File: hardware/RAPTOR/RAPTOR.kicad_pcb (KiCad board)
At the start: 2 copper layers, 88.9 x 53.3 mm, 47 parts, among them J1 SOLC_CONN, J10 EXT_LED3, J11 SRVOL_CONN, J12 SRVOR_CONN, J13 HOTWIRE_CONN, J14 RBF_CONN, J15 EEPROM_BTN_CONN, J16 SOLC_SW_CONN, J17 SOLP_SW_CONN, J2 SOLP_CONN, J3 JST_2MM_MALE, J4 CONN_LED_FIX, J5 CONN_SOLP_LED, J6 CONN_SOLC_LED, J7 EXT_LED0, J8 EXT_LED1, J9 EXT_LED2, P1 Power, P2 Analog, P3 Digital, P4 Digital, P5 CONN_01X01, P6 CONN_01X01, P7 CONN_01X01, P8 CONN_01X01, Q1 MOSFET-NCH-2N7002PW, Q2 MOSFET-NCH-2N7002PW, Q3 MOSFET-NCH-2N7002PW, Q4 MOSFET-NCH-2N7002PW, Q5 MOSFET-NCH-2N7002PW, U1 BMP280 Breakout, U2 BNO055 Breakout, U3 OpenLog, U4 AdafruitGPS, U5 U3V12F12, U6 D24V550F5

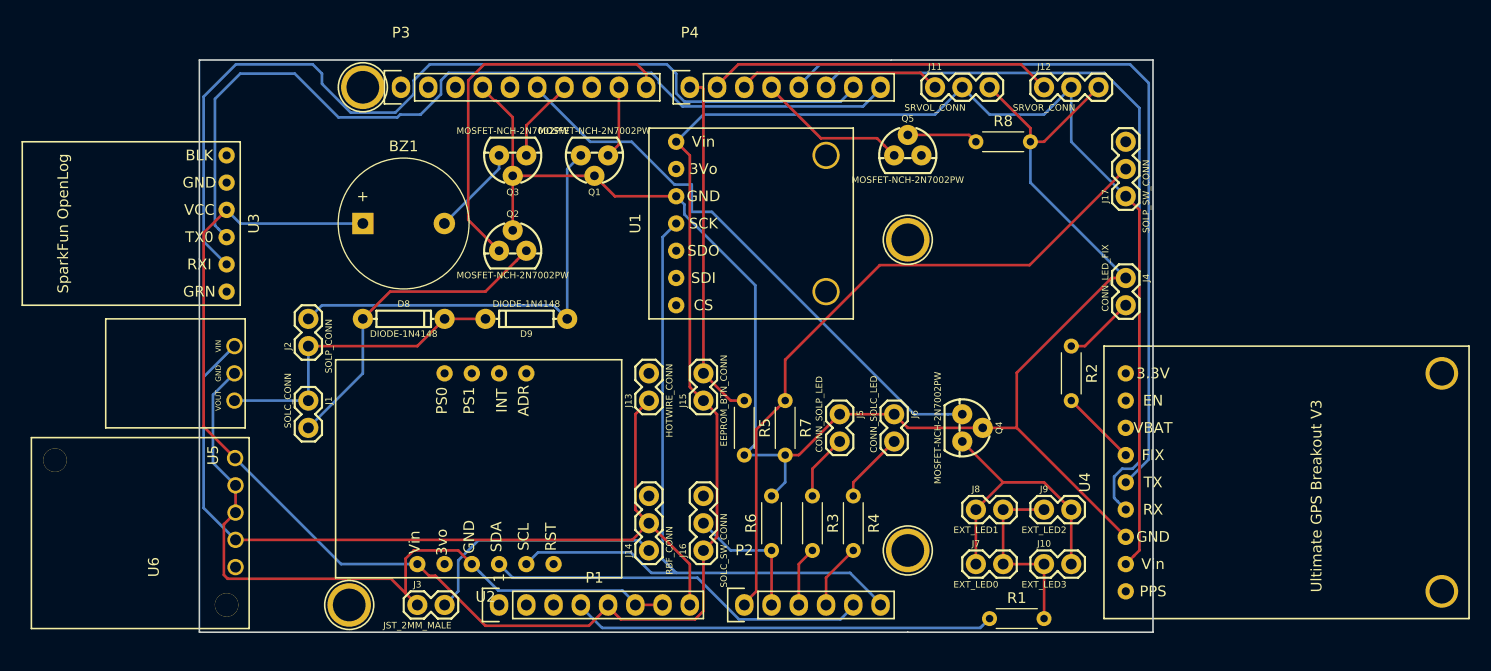
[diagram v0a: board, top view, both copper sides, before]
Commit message: Version 1 of fully wired PCB
A preliminary full connection of the PCB board
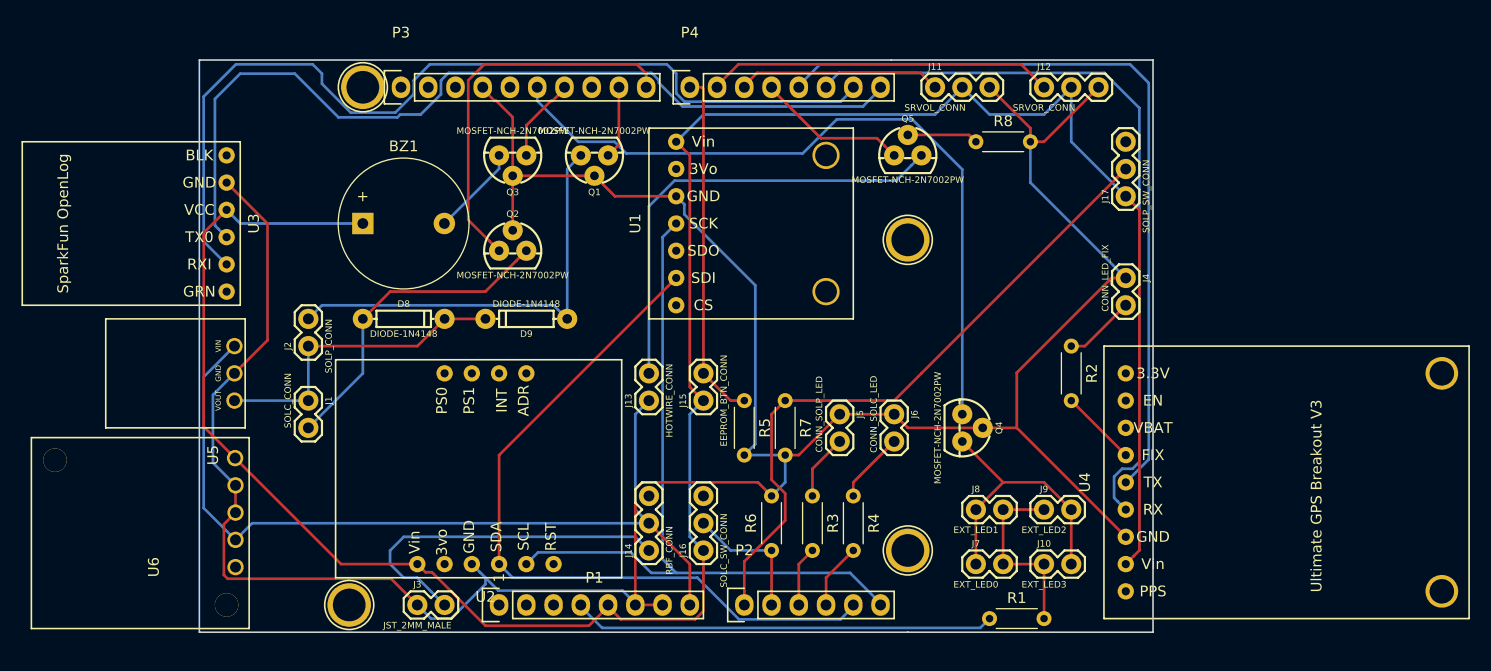
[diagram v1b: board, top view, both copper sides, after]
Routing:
- net GND: track 225.1 -> 268.3 mm
- net Net-(J13-Pad2): track 0.00 -> 42.9 mm
- net /I2C_SDA: track 35.8 -> 69.3 mm
- net /LEDS_DTA: track 53.8 -> 69.1 mm
- net Net-(J14-Pad1): track 23.6 -> 33.1 mm

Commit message: Revert "Revert "Widened PCB Board""
This reverts commit edbbf49bd2c69fdd694dc2b23b572114c8313dd8.
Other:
- board size 88.9 x 53.3 mm -> 88.9 x 55.9 mm
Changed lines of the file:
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@@
   (general
     (thickness 1.6)
-    (drawings 24)
+    (drawings 28)
     (tracks 313)
     (zones 0)
@@
       (net 24 "Net-(J14-Pad1)") (solder_mask_margin 0.1016))
   )
-  (gr_line (start 199.898 73.025) (end 175.514 73.025) (layer Edge.Cuts) (width 0.15))
+  (gr_line (start 110.998 71.755) (end 110.998 73.025) (layer Edge.Cuts) (width 0.15))
+  (gr_line (start 199.898 71.755) (end 199.898 73.025) (layer Edge.Cuts) (width 0.15))
+  (gr_line (start 199.898 126.365) (end 199.898 127.635) (layer Edge.Cuts) (width 0.15))
+  (gr_line (start 110.998 126.365) (end 110.998 127.635) (layer Edge.Cuts) (width 0.15))
+  (gr_line (start 199.898 71.755) (end 175.514 71.755) (layer Edge.Cuts) (width 0.15))
   (gr_line (start 199.898 126.365) (end 199.898 73.025) (layer Edge.Cuts) (width 0.15))
-  (gr_line (start 177.038 126.365) (end 199.898 126.365) (layer Edge.Cuts) (width 0.15))
+  (gr_line (start 177.038 127.635) (end 199.898 127.635) (layer Edge.Cuts) (width 0.15))
   (gr_text 1 (at 138.938 121.285 90) (layer F.SilkS)
     (effects (font (size 1 1) (thickness 0.15)))
@@
   (gr_line (start 114.427 74.93) (end 120.269 74.93) (angle 90) (layer Dwgs.User) (width 0.15))
   (gr_line (start 120.523 93.98) (end 104.648 93.98) (angle 90) (layer Dwgs.User) (width 0.15))
-  (gr_line (start 110.998 126.365) (end 177.038 126.365) (angle 90) (layer Edge.Cuts) (width 0.15))
+  (gr_line (start 110.998 127.635) (end 177.038 127.635) (angle 90) (layer Edge.Cuts) (width 0.15))
   (gr_line (start 110.998 73.025) (end 110.998 126.365) (angle 90) (layer Edge.Cuts) (width 0.15))
-  (gr_line (start 175.514 73.025) (end 110.998 73.025) (angle 90) (layer Edge.Cuts) (width 0.15))
+  (gr_line (start 175.514 71.755) (end 110.998 71.755) (angle 90) (layer Edge.Cuts) (width 0.15))
   (gr_line (start 173.355 102.235) (end 173.355 94.615) (angle 90) (layer Dwgs.User) (width 0.15))
   (gr_line (start 178.435 102.235) (end 173.355 102.235) (angle 90) (layer Dwgs.User) (width 0.15))

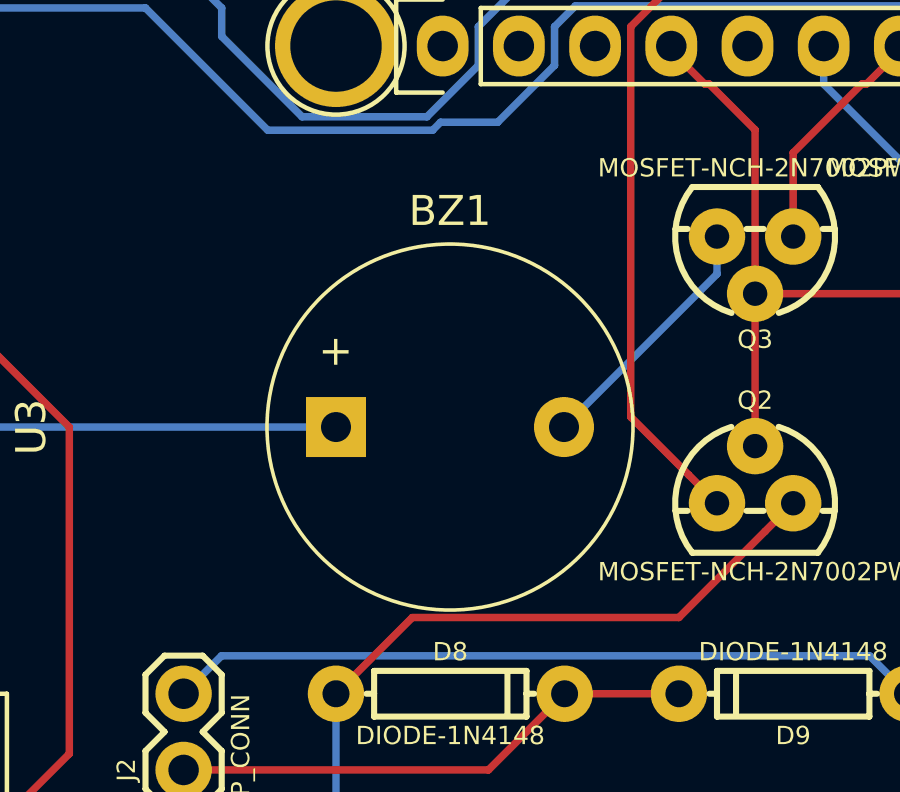
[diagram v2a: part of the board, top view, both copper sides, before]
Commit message: add connector for buzzer, resolves #72
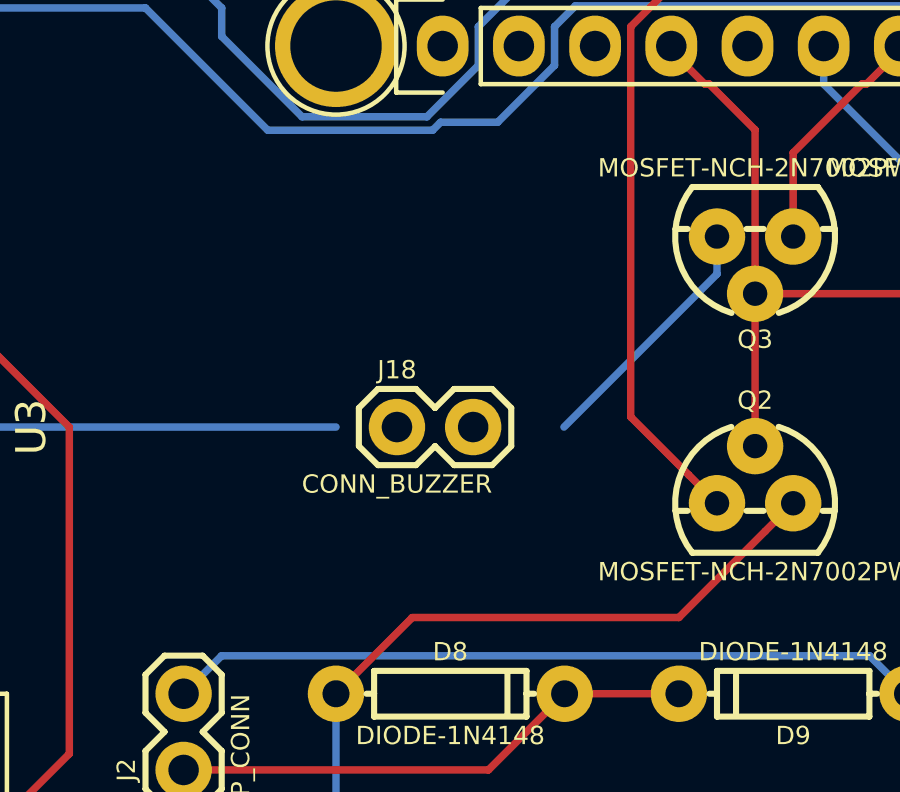
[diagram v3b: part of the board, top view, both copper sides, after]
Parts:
- removed BZ1: Buzzer, Buzzer_Beeper:Buzzer_12x9.5RM7.6
- added J18: CONN_BUZZER, Connectors:1X02, F.Cu at (128.3, 88.3)

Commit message: DeTrced the boi
See above
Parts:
- R1, R2, R3, R4, R5, R6, R7, R8: footprint Resistor_THT:R_Axial_DIN0204_L3.6mm_D1.6mm_P5.08mm_Horizontal -> Resistor_THT:R_Axial_DIN0411_L9.9mm_D3.6mm_P12.70mm_Horizontal
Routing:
- net GND: track 268.3 -> 0.00 mm
- net +5V: track 225.1 -> 0.00 mm
- net /SD_RX: track 86.5 -> 0.00 mm
- net /SD_TX: track 82.8 -> 0.00 mm
- net +7.5V: track 81.3 -> 0.00 mm
- net /GPS_TX: track 72.4 -> 0.00 mm
- net /GPS_RX: track 70.8 -> 0.00 mm
- net /I2C_SDA: track 69.3 -> 0.00 mm
- net /I2C_SCL: track 69.2 -> 0.00 mm
- net /LEDS_DTA: track 69.1 -> 0.00 mm
- net /SOLP_SW: track 63.9 -> 0.00 mm
- net Net-(J13-Pad2): track 42.9 -> 0.00 mm
- net Net-(D9-PadA): track 40.9 -> 0.00 mm
- net +3V3: track 39.6 -> 0.00 mm
- net /SOLC_DTA: track 35.9 -> 0.00 mm
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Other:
- board size 88.9 x 55.9 mm -> 91.4 x 55.9 mm

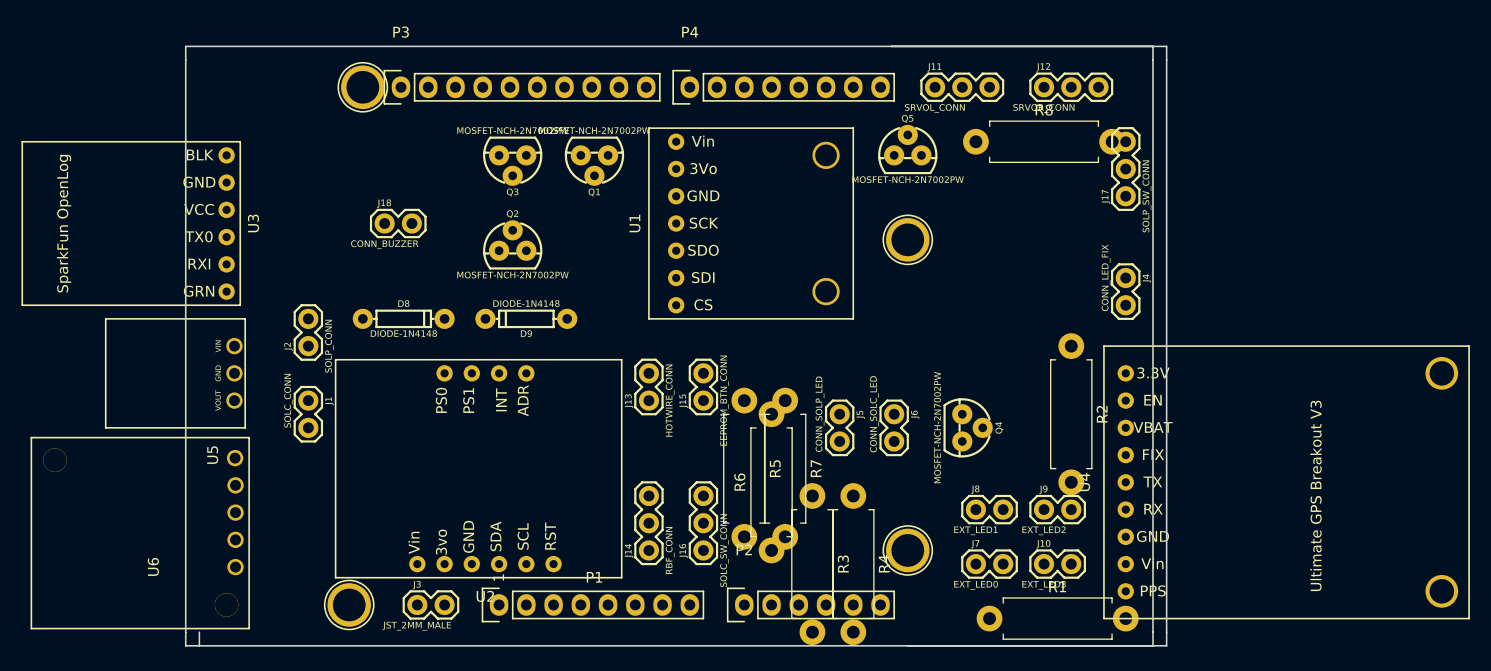
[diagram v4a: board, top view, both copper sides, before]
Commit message: Moved Breakouts to fully on board
Yeet
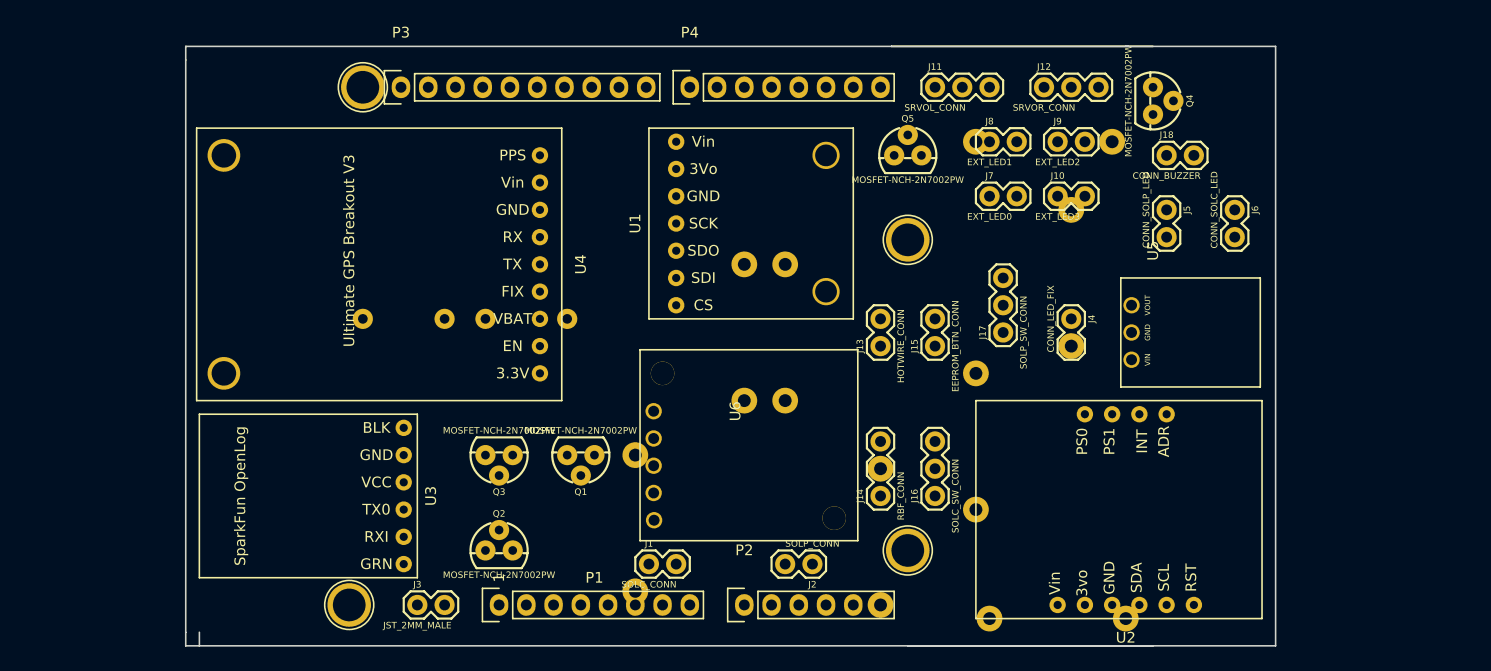
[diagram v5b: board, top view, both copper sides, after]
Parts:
- D8, D9, R1, R2, R3, R4, R5, R6, R7, R8: moved to B.Cu
- moved U5 89.7 mm to (199.9, 90.8), turned to 270 degrees
- moved J18 73.2 mm to (201.2, 81.9)
- moved U2 59.8 mm to (197.4, 123.8)
- moved U4 58.3 mm to (142.7, 92.1), turned to 90 degrees
- moved J2 51.2 mm to (168.1, 120.0), turned to 180 degrees
- moved U6 46.0 mm to (154.2, 102.2), turned to 270 degrees
- moved J6 37.0 mm to (207.5, 87.0)
- moved J5 35.9 mm to (201.2, 87.0)
- moved Q4 35.3 mm to (199.9, 76.8)
- moved J1 35.2 mm to (152.9, 120.0), turned to 0 degrees
- moved J10 34.3 mm to (191.0, 85.7)
- moved J7 34.3 mm to (184.7, 85.7)
- moved J8 34.3 mm to (184.7, 80.6)
- moved J9 34.3 mm to (191.0, 80.6)
- moved U3 30.3 mm to (130.0, 114.9)
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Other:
- board size 91.4 x 55.9 mm -> 101.6 x 55.9 mm

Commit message: Route Test
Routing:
- net GND: track 0.00 -> 5.08 mm
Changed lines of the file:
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@@
     (thickness 1.6)
     (drawings 29)
-    (tracks 0)
+    (tracks 1)
     (zones 0)
     (modules 47)
@@
   (gr_line (start 120.523 82.55) (end 120.523 93.98) (angle 90) (layer Dwgs.User) (width 0.15))
   (gr_line (start 104.648 82.55) (end 120.523 82.55) (angle 90) (layer Dwgs.User) (width 0.15))
+  (segment (start 138.938 116.84) (end 138.938 111.76) (width 0.25) (layer F.Cu) (net 4))
 )
